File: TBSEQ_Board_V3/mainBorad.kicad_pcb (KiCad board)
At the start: 2 copper layers, 200 x 130.3 mm, 262 parts, among them IC1 NJM2125F-TE1, IC12 4066, IC2 NJM2125F-TE1, IC3 74AHC1G04W5-7, IC4 NJM2125F-TE1, IC5 NJM2125F-TE1, J10 Conn_01x05, J11 Conn_01x05, J12 Conn_01x02, J13 Conn_01x01_Pin, J14 Conn_01x05, J3 Conn_01x02_Pin, J4 Conn_01x02, J5 Conn_01x02, J6 MJ-462, J7 Conn_01x03_Pin, J8 Conn_01x02_Pin, Q1 NPN, Q10 PNP, Q11 NPN, Q12 HN1C01FU-GR,LF, Q13 NPN, Q14 NPN, Q15 NPN, Q16 NPN, Q17 NPN, Q18 NPN, Q19 NPN, Q2 PNP, Q20 NPN, Q21 HN1C01FU-GR,LF, Q22 HN1C01FU-GR,LF, Q23 NPN, Q24 NPN, Q25 NPN, Q26 HN1C01FU-GR,LF, Q27 PNP, Q28 NJFET, Q29 NPN, Q30 NPN, Q35 NPN, Q36 PNP, Q37 NPN, Q38 PNP, Q39 NJFET, Q4 2SC3325-Y, Q40 NPN, Q41 NPN, Q8 PNP, Q9 PNP, SW1 2MS1T1B4VS2QES, U1 LM13700

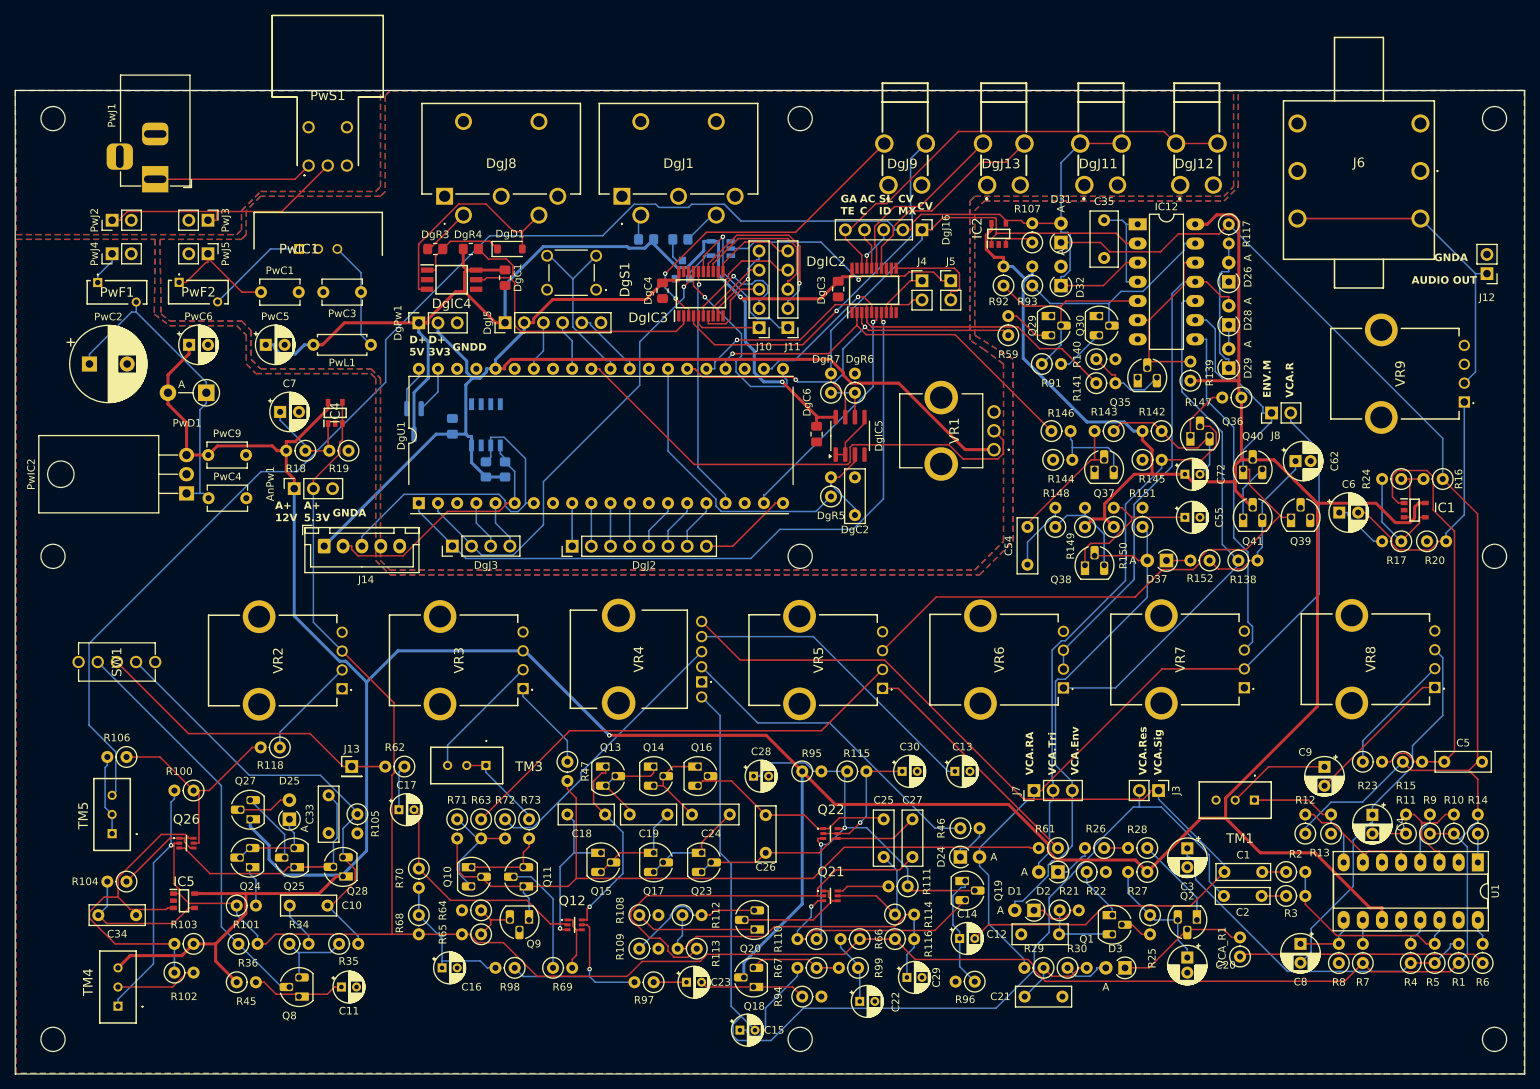
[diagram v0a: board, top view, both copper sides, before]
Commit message: V3Board
スペーサー穴追加
オートルーター後
DualTr,OPアンプは表面実装に切り替え
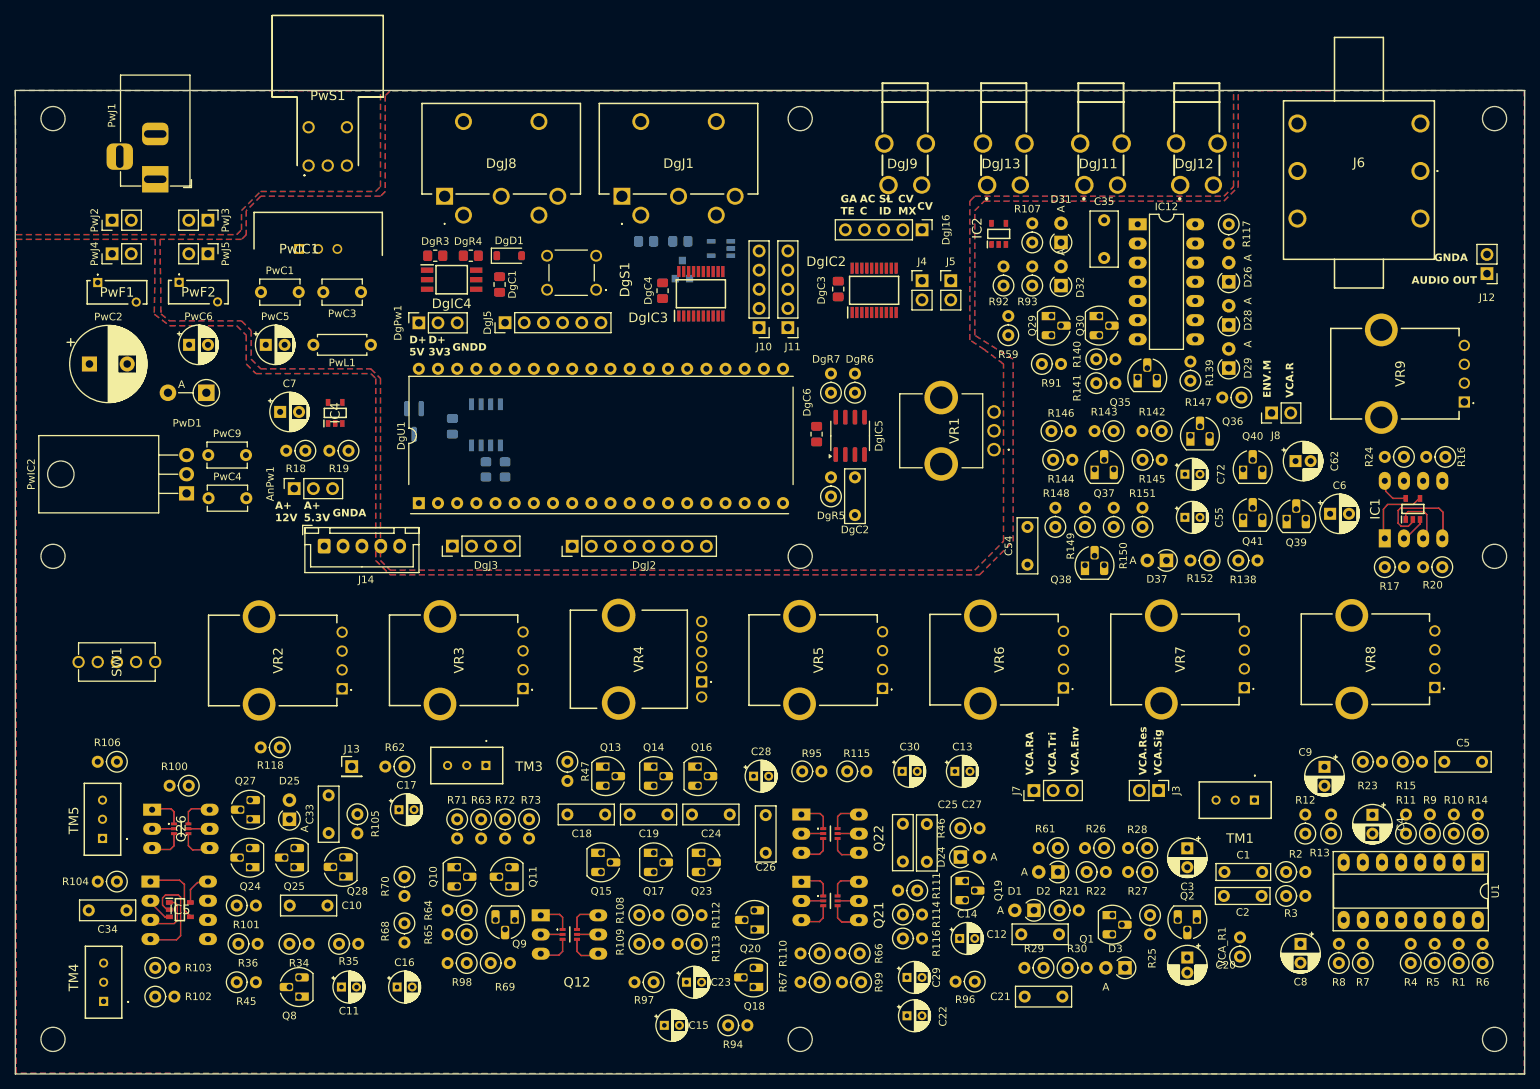
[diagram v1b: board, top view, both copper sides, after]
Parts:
- IC1, IC5: value NJM2125F-TE1 -> NJM2125F-TE1_DIP8; footprint SamacSys_Parts:SOT95P280X130-5N -> SamacSys_Parts:NJM2125F-SOT95&DIP8
- Q12, Q21, Q22, Q26: footprint SamacSys_Parts:HN1C01FUGRLF -> SamacSys_Parts:HN1C01FUGRLF_SOT23&DIP8
- moved R94 10.5 mm to (118.5, 144.1)
- moved C15 10.0 mm to (110.0, 144.1)
- moved R69 8.28 mm to (87.0, 135.9)
- moved C22 6.54 mm to (142.1, 142.9)
- moved C16 6.48 mm to (74.6, 139.1)
- moved R98 6.38 mm to (83.8, 135.9)
- moved R103 5.99 mm to (42.5, 136.5), turned to 0 degrees
- moved R102 4.07 mm to (42.5, 140.3)
- moved R17 4.06 mm to (205.5, 83.4), turned to 0 degrees
- moved R20 3.98 mm to (213.1, 83.4), turned to 180 degrees
- moved R16 2.95 mm to (213.5, 68.8)
- moved R24 2.95 mm to (208.0, 68.8)
- moved C25 2.61 mm to (141.6, 117.4)
- moved R68 2.19 mm to (75.6, 130.6)
- moved R70 2.19 mm to (75.6, 124.5)
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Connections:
- IC1 pad 1: Net-(IC1-+INPUT) -> Net-(IC1-OUTPUT)
- IC1 pad 2: GNDA -> Net-(IC1--INPUT)
- IC1 pad 3: Net-(IC1--INPUT) -> Net-(IC1-+INPUT)
- IC1 pad 4: Net-(IC1-OUTPUT) -> GNDA
- IC1 pad 5: A+12V -> unconnected-(IC1-NC-Pad5)
- IC5 pad 1: A+5.333V -> Net-(IC5-OUTPUT)
- IC5 pad 2: GNDA -> Net-(IC5--INPUT)
- IC5 pad 3: Net-(IC5--INPUT) -> A+5.333V
- IC5 pad 4: Net-(IC5-OUTPUT) -> GNDA
- IC5 pad 5: A+12V -> unconnected-(IC5-NC-Pad5)
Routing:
- net A+12V: track 563.5 -> 0.00 mm, vias 1 -> 0
- net A+5.333V: track 470.5 -> 0.00 mm, vias 1 -> 0
- net A+VCO_CV: track 220.6 -> 0.00 mm
- net D+3.3V: track 159.3 -> 0.00 mm
- net D+5V: track 156.0 -> 0.00 mm, vias 2 -> 0
- net A+VCA_Resonance: track 142.3 -> 0.00 mm
- net A+VCA_Signal: track 122.1 -> 0.00 mm
- net A+VCA-Reso_ACC: track 103.7 -> 0.00 mm
- net Net-(Q10-C): track 102.5 -> 0.00 mm
- net A+ENV.MOD: track 98.7 -> 0.00 mm
- net D+3.3V_MIDITX: track 93.5 -> 0.00 mm, vias 1 -> 0
- net A+VCA_Trig: track 74.0 -> 0.00 mm
- net Net-(VR6-CCW): track 69.6 -> 0.00 mm
- net A+VCA_Env: track 69.0 -> 0.00 mm
- net A+TEMPO: track 66.7 -> 0.00 mm
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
